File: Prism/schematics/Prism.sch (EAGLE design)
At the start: 151 parts, among them IC100 LD1117S50, IC110 LD1117S33, IC3 TL074D, IC4 CS4271, IC5 NE5532D, IC6 NE5532D, IC7 LM317, IC9 N25Q128A13, U1 STM32F427V(100PIN), X2 53048-05, Y1 24.576MHz, Y2 8MHz

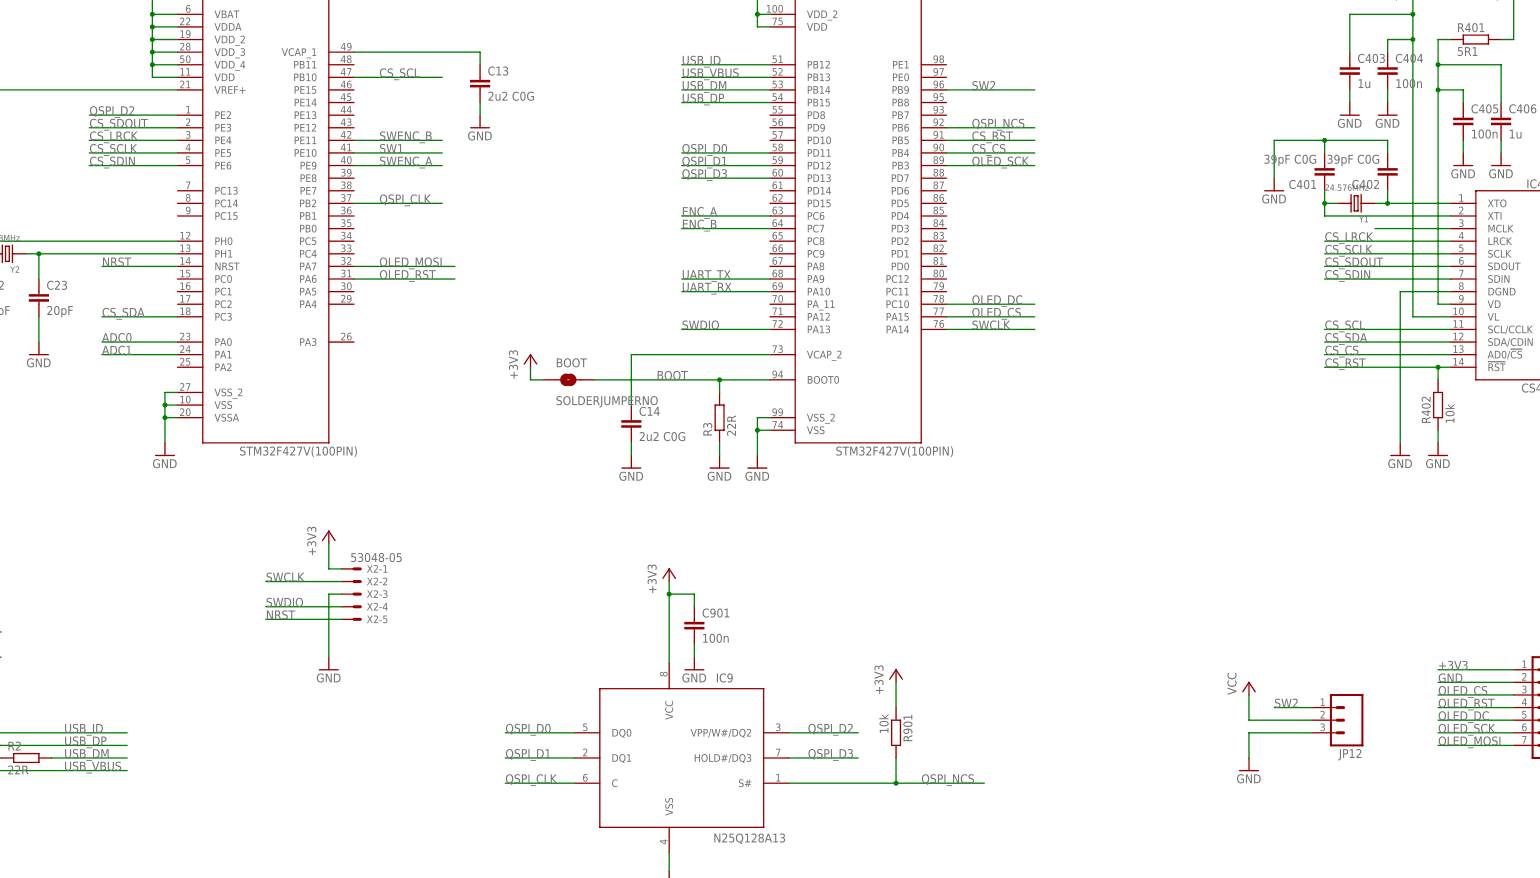
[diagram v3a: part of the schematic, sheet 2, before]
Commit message: finished Prism F4 udpate, had to move FLASH to normal SPI and re track
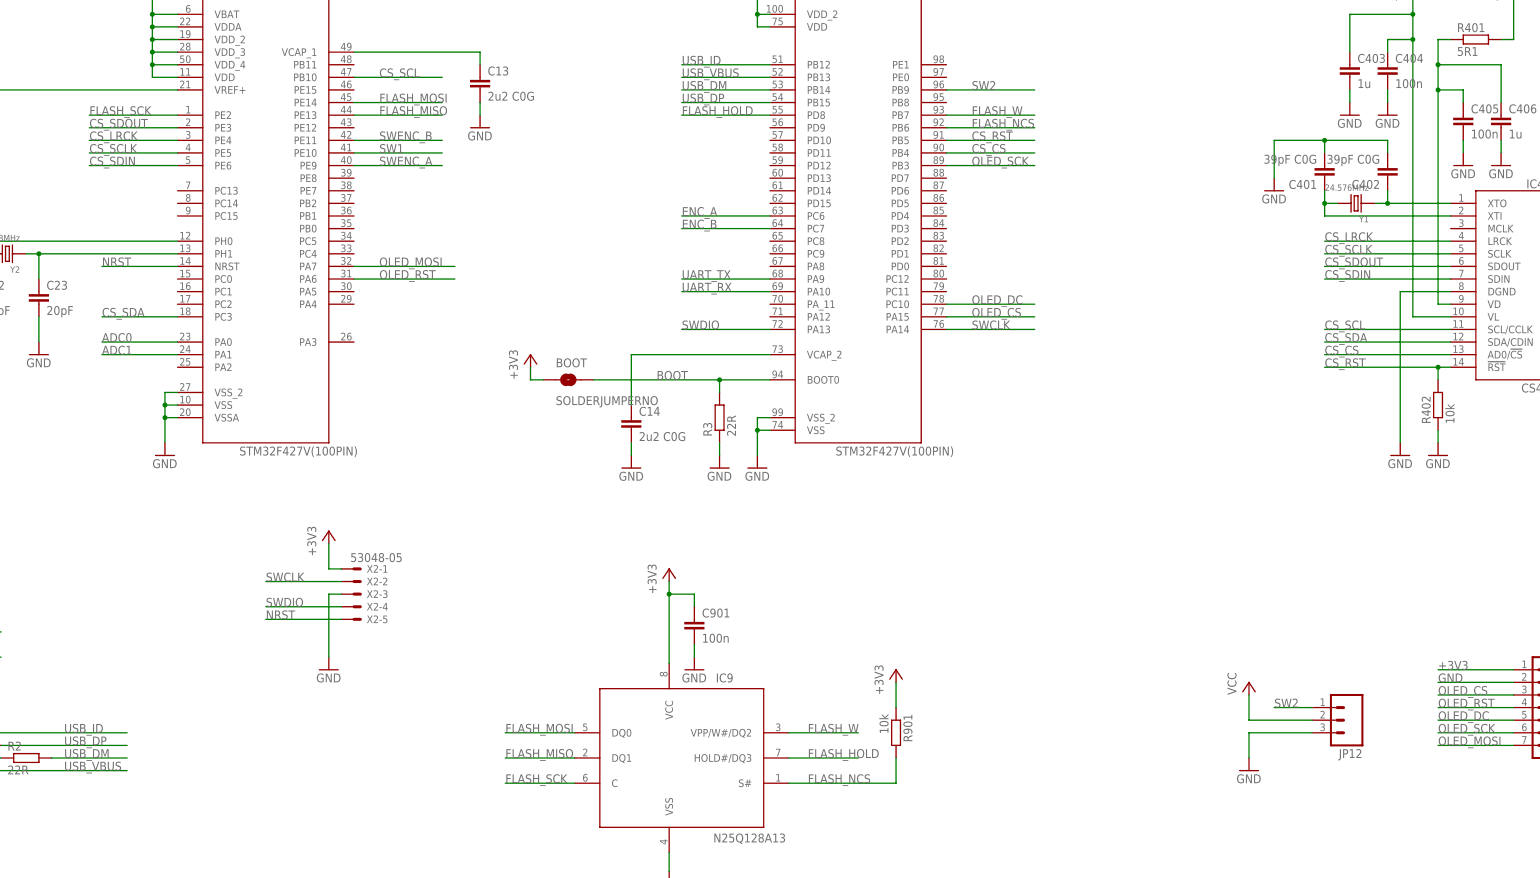
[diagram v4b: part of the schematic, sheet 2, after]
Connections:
- net QSPI_NCS renamed FLASH_NCS
- removed net CS_MCLK: IC4.MCLK
- removed net QSPI_CLK: IC9.C, U1A.PB2
- removed net QSPI_D0: IC9.DQ0, U1B.PD11
- removed net QSPI_D1: IC9.DQ1, U1B.PD12
- removed net QSPI_D2: IC9.VPP/W#/DQ2, U1A.PE2
- removed net QSPI_D3: IC9.HOLD#/DQ3, U1B.PD13
- new net FLASH_HOLD: IC9.HOLD#/DQ3, U1B.PD8
- new net FLASH_MISO: IC9.DQ1, U1A.PE13
- new net FLASH_MOSI: IC9.DQ0, U1A.PE14
- new net FLASH_SCK: IC9.C, U1A.PE2
- new net FLASH_W: IC9.VPP/W#/DQ2, U1B.PB7
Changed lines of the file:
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@@
 </segment>
 </net>
-<net name="QSPI_NCS" class="0">
+<net name="FLASH_NCS" class="0">
 <segment>
 <pinref part="IC9" gate="N25Q128A13" pin="S#"/>
 <wire x1="222.25" y1="5.08" x2="243.84" y2="5.08" width="0.1524" layer="91"/>
-<label x="248.92" y="5.08" size="1.778" layer="95"/>
-<wire x1="243.84" y1="5.08" x2="261.62" y2="5.08" width="0.1524" layer="91"/>
+<label x="226.06" y="5.08" size="1.778" layer="95"/>
 <wire x1="243.84" y1="5.08" x2="243.84" y2="10.16" width="0.1524" layer="91"/>
 <pinref part="R901" gate="G$1" pin="2"/>
-<junction x="243.84" y="5.08"/>
 </segment>
 <segment>
@@
 </segment>
 </net>
-<net name="QSPI_D2" class="0">
+<net name="FLASH_W" class="0">
 <segment>
 <pinref part="IC9" gate="N25Q128A13" pin="VPP/W#/DQ2"/>
@@
 </segment>
 <segment>
-<wire x1="99.06" y1="139.7" x2="81.28" y2="139.7" width="0.1524" layer="91"/>
-<label x="81.28" y="139.7" size="1.778" layer="95"/>
-<pinref part="U1" gate="A" pin="PE2"/>
-</segment>
-</net>
-<net name="QSPI_D0" class="0">
+<pinref part="U1" gate="B" pin="PB7"/>
+<wire x1="254" y1="139.7" x2="271.78" y2="139.7" width="0.1524" layer="91"/>
+<label x="259.08" y="139.7" size="1.778" layer="95"/>
+</segment>
+</net>
+<net name="FLASH_MOSI" class="0">
 <segment>
 <pinref part="IC9" gate="N25Q128A13" pin="DQ0"/>
@@
 </segment>
 <segment>
-<wire x1="218.44" y1="132.08" x2="200.66" y2="132.08" width="0.1524" layer="91"/>
-<label x="200.66" y="132.08" size="1.778" layer="95"/>
-<pinref part="U1" gate="B" pin="PD11"/>
-</segment>
-</net>
-<net name="QSPI_D1" class="0">
+<wire x1="134.62" y1="142.24" x2="152.4" y2="142.24" width="0.1524" layer="91"/>
+<label x="139.7" y="142.24" size="1.778" layer="95"/>
+<pinref part="U1" gate="A" pin="PE14"/>
+</segment>
+</net>
+<net name="FLASH_MISO" class="0">
 <segment>
 <pinref part="IC9" gate="N25Q128A13" pin="DQ1"/>
@@
 </segment>
 <segment>
-<wire x1="218.44" y1="129.54" x2="200.66" y2="129.54" width="0.1524" layer="91"/>
-<label x="200.66" y="129.54" size="1.778" layer="95"/>
-<pinref part="U1" gate="B" pin="PD12"/>
-</segment>
-</net>
-<net name="QSPI_CLK" class="0">
-<segment>
-<pinref part="IC9" gate="N25Q128A13" pin="C"/>
-<wire x1="179.07" y1="5.08" x2="165.1" y2="5.08" width="0.1524" layer="91"/>
-<label x="165.1" y="5.08" size="1.778" layer="95"/>
-</segment>
-<segment>
-<wire x1="134.62" y1="121.92" x2="152.4" y2="121.92" width="0.1524" layer="91"/>
-<label x="139.7" y="121.92" size="1.778" layer="95"/>
-<pinref part="U1" gate="A" pin="PB2"/>
-</segment>
-</net>
-<net name="QSPI_D3" class="0">
-<segment>
-<wire x1="218.44" y1="127" x2="200.66" y2="127" width="0.1524" layer="91"/>
-<label x="200.66" y="127" size="1.778" layer="95"/>
-<pinref part="U1" gate="B" pin="PD13"/>
-</segment>
+<pinref part="U1" gate="A" pin="PE13"/>
+<wire x1="134.62" y1="139.7" x2="152.4" y2="139.7" width="0.1524" layer="91"/>
+<label x="139.7" y="139.7" size="1.778" layer="95"/>
+</segment>
+</net>
+<net name="FLASH_HOLD" class="0">
 <segment>
 <pinref part="IC9" gate="N25Q128A13" pin="HOLD#/DQ3"/>
 <wire x1="222.25" y1="10.16" x2="236.22" y2="10.16" width="0.1524" layer="91"/>
 <label x="226.06" y="10.16" size="1.778" layer="95"/>
+</segment>
+<segment>
+<pinref part="U1" gate="B" pin="PD8"/>
+<wire x1="218.44" y1="139.7" x2="200.66" y2="139.7" width="0.1524" layer="91"/>
+<label x="200.66" y="139.7" size="1.778" layer="95"/>
 </segment>
 </net>
@@
 </segment>
 </net>
-<net name="CS_MCLK" class="0">
-<segment>
-<pinref part="IC4" gate="CS4271" pin="MCLK"/>
-<wire x1="355.6" y1="116.84" x2="340.36" y2="116.84" width="0.1524" layer="91"/>
+<net name="FLASH_SCK" class="0">
+<segment>
+<wire x1="99.06" y1="139.7" x2="81.28" y2="139.7" width="0.1524" layer="91"/>
+<label x="81.28" y="139.7" size="1.778" layer="95"/>
+<pinref part="U1" gate="A" pin="PE2"/>
+</segment>
+<segment>
+<pinref part="IC9" gate="N25Q128A13" pin="C"/>
+<wire x1="179.07" y1="5.08" x2="165.1" y2="5.08" width="0.1524" layer="91"/>
+<label x="165.1" y="5.08" size="1.778" layer="95"/>
 </segment>
 </net>
@@
 </sheet>
 </sheets>
+<errors>
+</errors>
 </schematic>
 </drawing>

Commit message: latest produced version of prism
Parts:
- C13, C14: value 2u2 C0G -> 2u2
- R602, R605, R609, R612: value 4k3 -> 5k6
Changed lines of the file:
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@@
 <?xml version="1.0" encoding="utf-8"?>
 <!DOCTYPE eagle SYSTEM "eagle.dtd">
-<eagle version="7.6.0">
+<eagle version="7.5.0">
 <drawing>
 <settings>
@@
 <part name="R901" library="Rebel" deviceset="R-EU_" device="0603" value="10k"/>
 <part name="+3V5" library="supply1" deviceset="+3V3" device=""/>
-<part name="R602" library="Rebel" deviceset="R-EU_" device="0603" value="4k3"/>
-<part name="R605" library="Rebel" deviceset="R-EU_" device="0603" value="4k3"/>
+<part name="R602" library="Rebel" deviceset="R-EU_" device="0603" value="5k6"/>
+<part name="R605" library="Rebel" deviceset="R-EU_" device="0603" value="5k6"/>
 <part name="R603" library="Rebel" deviceset="R-EU_" device="0603" value="4k7"/>
 <part name="R606" library="Rebel" deviceset="R-EU_" device="0603" value="4k7"/>
@@
 <part name="P+2" library="supply1" deviceset="+12V" device=""/>
 <part name="P-1" library="supply1" deviceset="-12V" device=""/>
-<part name="R609" library="Rebel" deviceset="R-EU_" device="0603" value="4k3"/>
-<part name="R612" library="Rebel" deviceset="R-EU_" device="0603" value="4k3"/>
+<part name="R609" library="Rebel" deviceset="R-EU_" device="0603" value="5k6"/>
+<part name="R612" library="Rebel" deviceset="R-EU_" device="0603" value="5k6"/>
 <part name="R610" library="Rebel" deviceset="R-EU_" device="0603" value="4k7"/>
 <part name="R613" library="Rebel" deviceset="R-EU_" device="0603" value="4k7"/>
@@
 <part name="R4" library="Rebel" deviceset="R-EU_" device="0603" value="10k"/>
 <part name="GND77" library="supply1" deviceset="GND" device=""/>
-<part name="C13" library="Rebel" deviceset="C-EU" device="C0603" value="2u2 C0G"/>
-<part name="C14" library="Rebel" deviceset="C-EU" device="C0603" value="2u2 C0G"/>
+<part name="C13" library="Rebel" deviceset="C-EU" device="C0603" value="2u2"/>
+<part name="C14" library="Rebel" deviceset="C-EU" device="C0603" value="2u2"/>
 <part name="GND78" library="supply1" deviceset="GND" device=""/>
 <part name="GND79" library="supply1" deviceset="GND" device=""/>

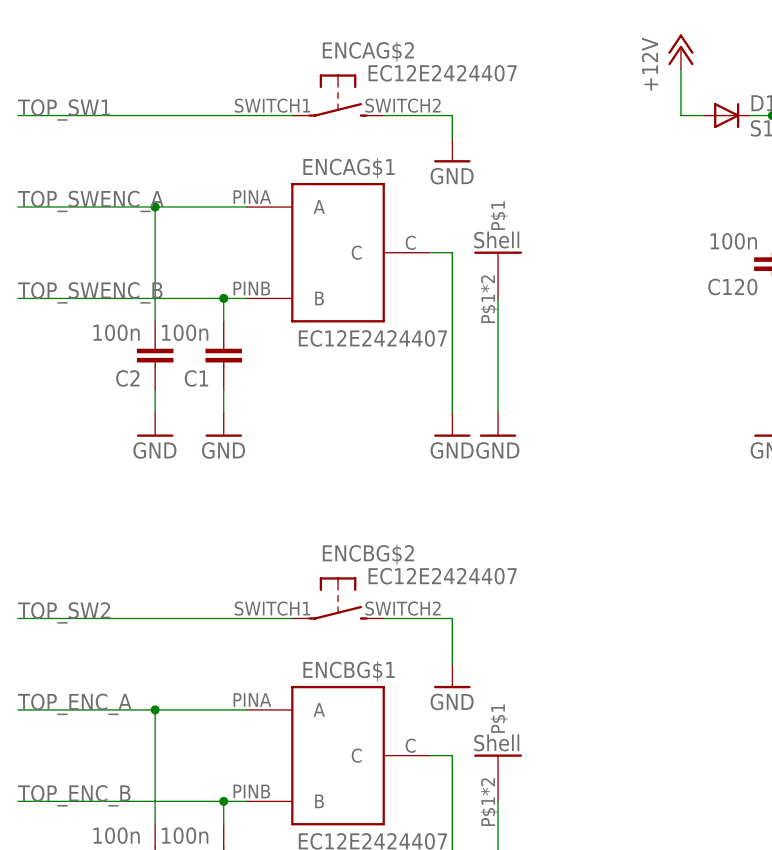
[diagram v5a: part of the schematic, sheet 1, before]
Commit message: renamed and updated to Prism Screen Rev04 - moved 5.5mm
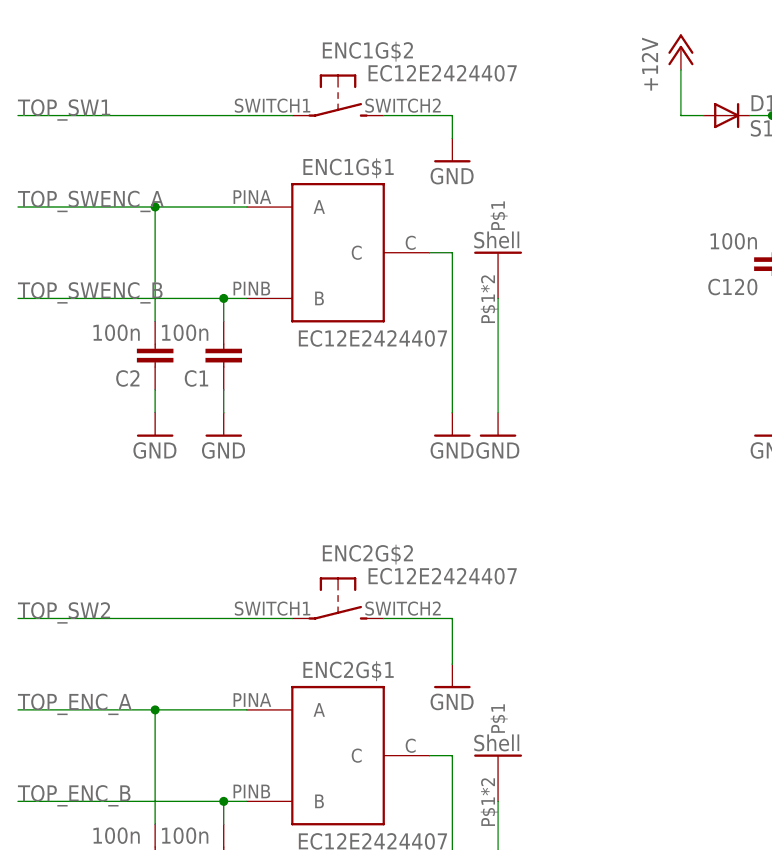
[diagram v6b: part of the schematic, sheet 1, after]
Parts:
- renumbered ENCA to ENC1, ENCB to ENC2
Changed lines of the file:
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@@
 <part name="GND30" library="supply1" deviceset="GND" device=""/>
 <part name="GND31" library="supply1" deviceset="GND" device=""/>
-<part name="ENCA" library="Rebel" deviceset="EC12E2424407" device=""/>
-<part name="ENCB" library="Rebel" deviceset="EC12E2424407" device=""/>
+<part name="ENC1" library="Rebel" deviceset="EC12E2424407" device=""/>
+<part name="ENC2" library="Rebel" deviceset="EC12E2424407" device=""/>
 <part name="R501" library="Rebel" deviceset="R-EU_" device="0603" value="20k"/>
 <part name="R504" library="Rebel" deviceset="R-EU_" device="0603" value="22k"/>
@@
 </plain>
 <instances>
-<instance part="ENCA" gate="G$1" x="35.56" y="307.34"/>
-<instance part="ENCB" gate="G$1" x="35.56" y="251.46"/>
-<instance part="ENCA" gate="G$2" x="35.56" y="322.58" rot="R270"/>
-<instance part="ENCA" gate="G$3" x="53.34" y="307.34"/>
-<instance part="ENCB" gate="G$2" x="35.56" y="266.7" rot="R270"/>
+<instance part="ENC1" gate="G$1" x="35.56" y="307.34"/>
+<instance part="ENC2" gate="G$1" x="35.56" y="251.46"/>
+<instance part="ENC1" gate="G$2" x="35.56" y="322.58" rot="R270"/>
+<instance part="ENC1" gate="G$3" x="53.34" y="307.34"/>
+<instance part="ENC2" gate="G$2" x="35.56" y="266.7" rot="R270"/>
 <instance part="IC7" gate="G$1" x="104.14" y="322.58"/>
 <instance part="R122" gate="G$1" x="104.14" y="297.18" rot="R90"/>
@@
 <instance part="JP5" gate="G$1" x="25.4" y="210.82" rot="R180"/>
 <instance part="JP11" gate="G$1" x="121.92" y="215.9" rot="R180"/>
-<instance part="ENCB" gate="G$3" x="53.34" y="251.46"/>
+<instance part="ENC2" gate="G$3" x="53.34" y="251.46"/>
 <instance part="GND9" gate="1" x="48.26" y="259.08"/>
 <instance part="JP10" gate="G$1" x="81.28" y="210.82" rot="R180"/>
@@
 </segment>
 <segment>
-<pinref part="ENCA" gate="G$3" pin="P$1"/>
+<pinref part="ENC1" gate="G$3" pin="P$1"/>
 <pinref part="GND69" gate="1" pin="GND"/>
 <wire x1="53.34" y1="289.56" x2="53.34" y2="302.26" width="0.1524" layer="91"/>
 </segment>
 <segment>
-<pinref part="ENCA" gate="G$1" pin="C"/>
+<pinref part="ENC1" gate="G$1" pin="C"/>
 <pinref part="GND70" gate="1" pin="GND"/>
 <wire x1="45.72" y1="307.34" x2="48.26" y2="307.34" width="0.1524" layer="91"/>
@@
 </segment>
 <segment>
-<pinref part="ENCB" gate="G$1" pin="C"/>
+<pinref part="ENC2" gate="G$1" pin="C"/>
 <pinref part="GND72" gate="1" pin="GND"/>
 <wire x1="45.72" y1="251.46" x2="48.26" y2="251.46" width="0.1524" layer="91"/>
@@
 </segment>
 <segment>
-<pinref part="ENCA" gate="G$2" pin="S"/>
+<pinref part="ENC1" gate="G$2" pin="S"/>
 <pinref part="GND88" gate="1" pin="GND"/>
 <wire x1="40.64" y1="322.58" x2="48.26" y2="322.58" width="0.1524" layer="91"/>
@@
 </segment>
 <segment>
-<pinref part="ENCB" gate="G$2" pin="S"/>
+<pinref part="ENC2" gate="G$2" pin="S"/>
 <pinref part="GND9" gate="1" pin="GND"/>
 <wire x1="40.64" y1="266.7" x2="48.26" y2="266.7" width="0.1524" layer="91"/>
@@
 </segment>
 <segment>
-<pinref part="ENCB" gate="G$3" pin="P$1"/>
+<pinref part="ENC2" gate="G$3" pin="P$1"/>
 <pinref part="GND71" gate="1" pin="GND"/>
 <wire x1="53.34" y1="246.38" x2="53.34" y2="233.68" width="0.1524" layer="91"/>
@@
 </segment>
 <segment>
-<pinref part="ENCB" gate="G$2" pin="P"/>
+<pinref part="ENC2" gate="G$2" pin="P"/>
 <wire x1="30.48" y1="266.7" x2="0" y2="266.7" width="0.1524" layer="91"/>
 <label x="0" y="266.7" size="1.778" layer="95"/>
@@
 <net name="TOP_SWENC_B" class="0">
 <segment>
-<pinref part="ENCA" gate="G$1" pin="B"/>
+<pinref part="ENC1" gate="G$1" pin="B"/>
 <pinref part="C1" gate="G$1" pin="2"/>
 <wire x1="25.4" y1="302.26" x2="22.86" y2="302.26" width="0.1524" layer="91"/>
@@
 <net name="TOP_SWENC_A" class="0">
 <segment>
-<pinref part="ENCA" gate="G$1" pin="A"/>
+<pinref part="ENC1" gate="G$1" pin="A"/>
 <pinref part="C2" gate="G$1" pin="2"/>
 <wire x1="25.4" y1="312.42" x2="15.24" y2="312.42" width="0.1524" layer="91"/>
@@
 <net name="TOP_ENC_B" class="0">
 <segment>
-<pinref part="ENCB" gate="G$1" pin="B"/>
+<pinref part="ENC2" gate="G$1" pin="B"/>
 <pinref part="C3" gate="G$1" pin="2"/>
 <wire x1="25.4" y1="246.38" x2="22.86" y2="246.38" width="0.1524" layer="91"/>
@@
 <net name="TOP_ENC_A" class="0">
 <segment>
-<pinref part="ENCB" gate="G$1" pin="A"/>
+<pinref part="ENC2" gate="G$1" pin="A"/>
 <pinref part="C4" gate="G$1" pin="2"/>
 <wire x1="25.4" y1="256.54" x2="15.24" y2="256.54" width="0.1524" layer="91"/>
@@
 <net name="TOP_SW1" class="0">
 <segment>
-<pinref part="ENCA" gate="G$2" pin="P"/>
+<pinref part="ENC1" gate="G$2" pin="P"/>
 <wire x1="30.48" y1="322.58" x2="0" y2="322.58" width="0.1524" layer="91"/>
 <label x="0" y="322.58" size="1.778" layer="95"/>

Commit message: added 100nF to NRST
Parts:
- added C26: 100n, Rebel:C-EUC0603
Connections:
- net GND: now also C26.2
- net NRST: now also C26.1
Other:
- moved on the sheet: C22, C23, Y2
